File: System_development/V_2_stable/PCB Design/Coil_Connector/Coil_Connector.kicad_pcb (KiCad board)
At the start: 2 copper layers, 16.7 x 11.4 mm, 2 parts, among them J1 Conn_Coaxial

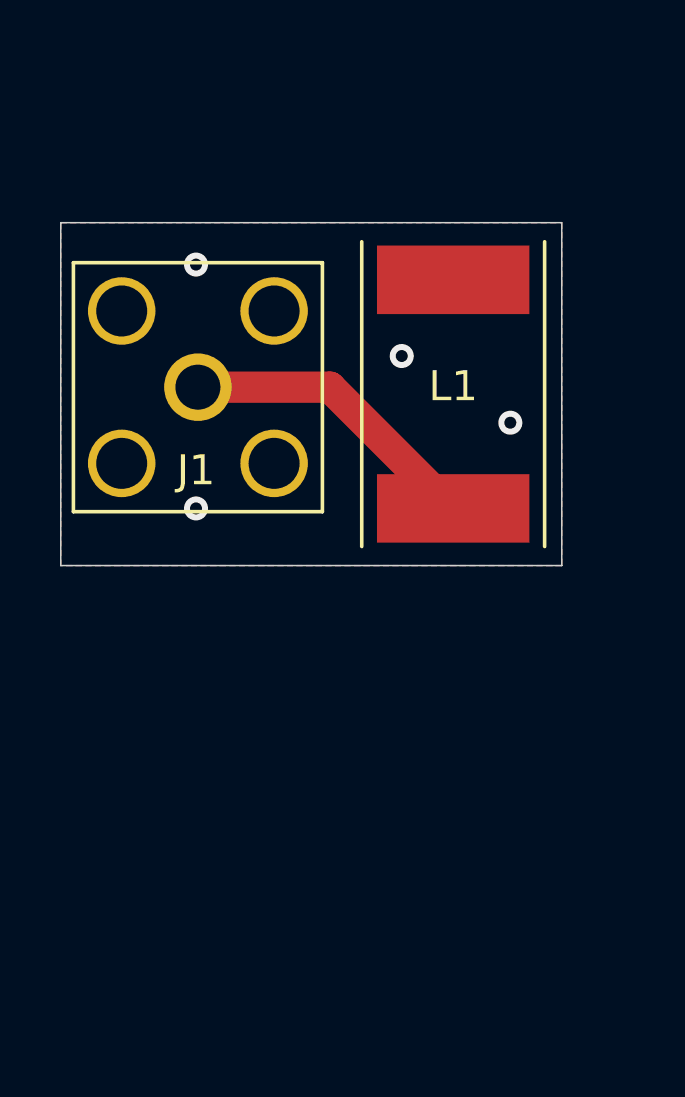
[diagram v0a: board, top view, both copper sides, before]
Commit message: Coil Connector PCB
Added screw holes
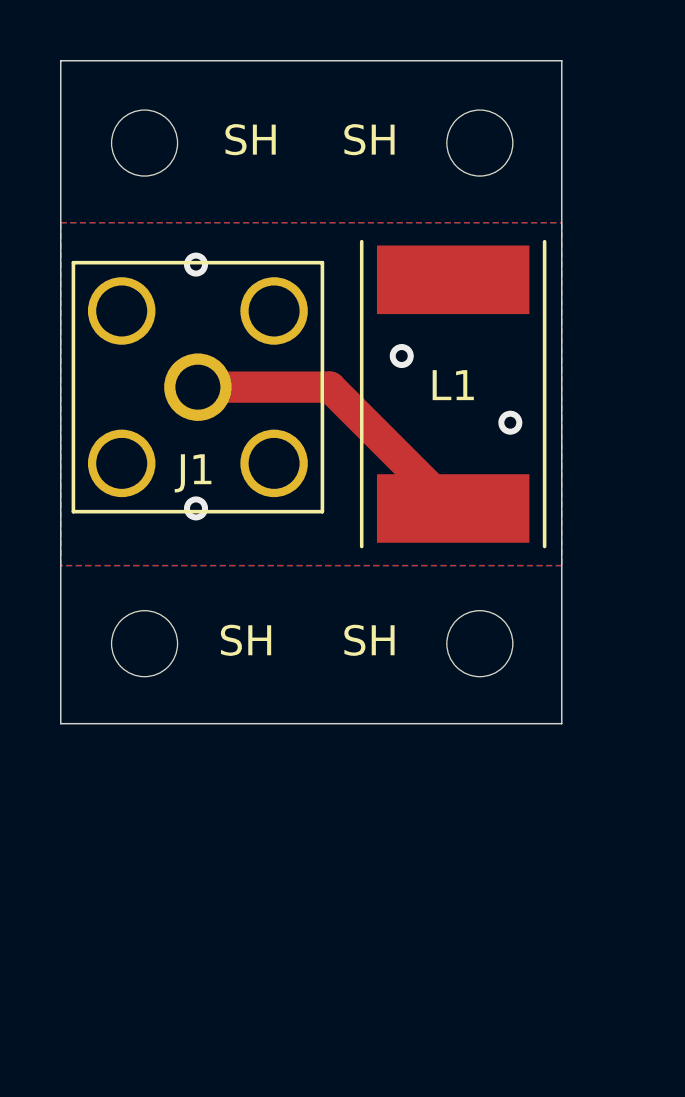
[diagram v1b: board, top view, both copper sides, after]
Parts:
- added SH: MountingHole_2.2mm_M2, MountingHole:MountingHole_2.2mm_M2, F.Cu at (144.8, 93.7)
- added SH: MountingHole_2.2mm_M2, MountingHole:MountingHole_2.2mm_M2, F.Cu at (133.6, 110.4)
- added SH: MountingHole_2.2mm_M2, MountingHole:MountingHole_2.2mm_M2, F.Cu at (133.6, 93.7)
- added SH: MountingHole_2.2mm_M2, MountingHole:MountingHole_2.2mm_M2, F.Cu at (144.8, 110.4)
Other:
- board size 16.7 x 11.4 mm -> 16.7 x 22.1 mm
- net class 50 Ohm removed
- net class Default removed

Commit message: Coil PCB & HP Amp PCB
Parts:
- removed the SH at (144.8, 93.7)
- removed the SH at (144.8, 110.4)
- moved SH 15.3 mm to (146.8, 101.3)
- moved SH 11.6 mm to (139.1, 120.7)
- moved L1 6.69 mm to (139.1, 109.5), turned to 180 degrees
- moved J1 3.70 mm to (139.1, 101.5)
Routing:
- net Net-(J1-Pad1): track 10.2 -> 6.98 mm
- net GND: vias 4 -> 3
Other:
- board size 16.7 x 22.1 mm -> 15.5 x 26.7 mm
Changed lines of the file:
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@@
   (net 2 "Net-(J1-Pad1)")
   (footprint "Connector_Coaxial:SMA_Amphenol_132203-12_Horizontal" (layer "F.Cu")
-    (at 135.382 101.813001)
+    (at 139.065 101.473)
     (descr "https://www.amphenolrf.com/media/downloads/1769/132203-12.pdf")
     (tags "SMA THT Female Jack Horizontal")
     (attr through_hole)
-    (fp_text reference "J1" (at -0.0635 2.771499 180) (layer "F.SilkS")
+    (fp_text reference "J1" (at -0.0635 -2.667 180) (layer "F.SilkS")
       (effects (font (size 1 1) (thickness 0.15)))
     )
@@
   )
   (footprint "L_Coil:L_Coil" (layer "F.Cu")
-    (at 143.891 104.8385)
+    (at 139.065 109.474 180)
     (attr through_hole)
     (fp_text reference "L1" (at 0 -3.056) (layer "F.SilkS")
@@
     (fp_line (start 3.302 2.54) (end -3.302 2.54) (layer "F.CrtYd") (width 0.12))
     (fp_line (start 3.302 -8.128) (end 3.302 2.54) (layer "F.CrtYd") (width 0.12))
-    (pad "1" smd rect locked (at 0 1.016) (size 5.08 2.286) (layers "F.Cu" "F.Paste" "F.Mask")
+    (pad "1" smd rect locked (at 0 1.016 180) (size 5.08 2.286) (layers "F.Cu" "F.Paste" "F.Mask")
       (net 2 "Net-(J1-Pad1)"))
-    (pad "2" smd rect locked (at 0 -6.604) (size 5.08 2.286) (layers "F.Cu" "F.Paste" "F.Mask")
+    (pad "2" smd rect locked (at 0 -6.604 180) (size 5.08 2.286) (layers "F.Cu" "F.Paste" "F.Mask")
       (net 1 "GND"))
   )
   (footprint "MountingHole:MountingHole_2.2mm_M2" (layer "F.Cu")
-    (at 144.78 93.6752)
-    (descr "Mounting Hole 2.2mm, no annular, M2")
-    (tags "mounting hole 2.2mm no annular m2")
-    (attr exclude_from_pos_files exclude_from_bom)
-    (fp_text reference "SH" (at -3.6576 -0.0762) (layer "F.SilkS")
-      (effects (font (size 1 1) (thickness 0.15)))
-    )
-    (fp_text value "MountingHole_2.2mm_M2" (at 0 3.2) (layer "F.Fab")
-      (effects (font (size 1 1) (thickness 0.15)))
-    )
-    (fp_text user "${REFERENCE}" (at 0.3 0) (layer "F.Fab")
-      (effects (font (size 1 1) (thickness 0.15)))
-    )
-    (fp_circle (center 0 0) (end 2.2 0) (layer "Cmts.User") (width 0.15) (fill none))
-    (fp_circle (center 0 0) (end 2.45 0) (layer "F.CrtYd") (width 0.05) (fill none))
-    (pad "" np_thru_hole circle (at 0 0) (size 2.2 2.2) (drill 2.2) (layers *.Cu *.Mask))
-  )
-  (footprint "MountingHole:MountingHole_2.2mm_M2" (layer "F.Cu")
-    (at 133.604 110.363)
+    (at 139.065 120.65)
     (descr "Mounting Hole 2.2mm, no annular, M2")
     (tags "mounting hole 2.2mm no annular m2")
@@
   )
   (footprint "MountingHole:MountingHole_2.2mm_M2" (layer "F.Cu")
-    (at 133.604 93.6752)
+    (at 146.812 101.346)
     (descr "Mounting Hole 2.2mm, no annular, M2")
     (tags "mounting hole 2.2mm no annular m2")
     (attr exclude_from_pos_files exclude_from_bom)
-    (fp_text reference "SH" (at 3.556 -0.0762) (layer "F.SilkS")
+    (fp_text reference "SH" (at 0 -3.302) (layer "F.SilkS")
       (effects (font (size 1 1) (thickness 0.15)))
     )
@@
     (pad "" np_thru_hole circle (at 0 0) (size 2.2 2.2) (drill 2.2) (layers *.Cu *.Mask))
   )
-  (footprint "MountingHole:MountingHole_2.2mm_M2" (layer "F.Cu")
-    (at 144.78 110.363)
-    (descr "Mounting Hole 2.2mm, no annular, M2")
-    (tags "mounting hole 2.2mm no annular m2")
-    (attr exclude_from_pos_files exclude_from_bom)
-    (fp_text reference "SH" (at -3.6576 -0.0762) (layer "F.SilkS")
-      (effects (font (size 1 1) (thickness 0.15)))
-    )
-    (fp_text value "MountingHole_2.2mm_M2" (at 0 3.2) (layer "F.Fab")
-      (effects (font (size 1 1) (thickness 0.15)))
-    )
-    (fp_text user "${REFERENCE}" (at 0.3 0) (layer "F.Fab")
-      (effects (font (size 1 1) (thickness 0.15)))
-    )
-    (fp_circle (center 0 0) (end 2.2 0) (layer "Cmts.User") (width 0.15) (fill none))
-    (fp_circle (center 0 0) (end 2.45 0) (layer "F.CrtYd") (width 0.05) (fill none))
-    (pad "" np_thru_hole circle (at 0 0) (size 2.2 2.2) (drill 2.2) (layers *.Cu *.Mask))
-  )
-  (gr_line (start 147.5105 113.03) (end 147.5105 90.932) (layer "Edge.Cuts") (width 0.05))
-  (gr_line (start 130.81 113.03) (end 147.5105 113.03) (layer "Edge.Cuts") (width 0.05))
-  (gr_line (start 130.81 90.932) (end 130.81 113.03) (layer "Edge.Cuts") (width 0.05))
-  (gr_line (start 147.5105 90.932) (end 130.81 90.932) (layer "Edge.Cuts") (width 0.05))
-  (via (at 145.796 102.997) (size 0.8) (drill 0.4) (layers "F.Cu" "B.Cu") (net 1))
-  (via (at 135.3185 97.7265) (size 0.8) (drill 0.4) (layers "F.Cu" "B.Cu") (net 1))
-  (via (at 135.3185 105.8545) (size 0.8) (drill 0.4) (layers "F.Cu" "B.Cu") (net 1))
-  (via (at 142.1765 100.7745) (size 0.8) (drill 0.4) (layers "F.Cu" "B.Cu") (net 1))
-  (segment (start 139.786001 101.813001) (end 143.891 105.918) (width 1.044) (layer "F.Cu") (net 2))
-  (segment (start 135.382 101.813001) (end 139.786001 101.813001) (width 1.044) (layer "F.Cu") (net 2))
+  (gr_line (start 149.606 96.774) (end 149.606 106.426) (layer "Edge.Cuts") (width 0.05))
+  (gr_line (start 149.606 106.426) (end 149.606 106.934) (layer "Edge.Cuts") (width 0.05))
+  (gr_line (start 144.018 106.934) (end 144.018 123.444) (layer "Edge.Cuts") (width 0.05))
+  (gr_line (start 134.112 96.774) (end 149.606 96.774) (layer "Edge.Cuts") (width 0.05))
+  (gr_line (start 144.018 123.444) (end 134.112 123.444) (layer "Edge.Cuts") (width 0.05))
+  (gr_line (start 149.606 106.934) (end 144.018 106.934) (layer "Edge.Cuts") (width 0.05))
+  (gr_line (start 134.112 123.444) (end 134.112 96.774) (layer "Edge.Cuts") (width 0.05))
+  (via (at 141.732 101.346) (size 0.8) (drill 0.4) (layers "F.Cu" "B.Cu") (free) (net 1))
+  (via (at 136.398 101.346) (size 0.8) (drill 0.4) (layers "F.Cu" "B.Cu") (free) (net 1))
+  (via (at 138.938 111.252) (size 0.8) (drill 0.4) (layers "F.Cu" "B.Cu") (free) (net 1))
+  (segment (start 139.065 101.473) (end 139.065 108.458) (width 1.044) (layer "F.Cu") (net 2))
   (zone (net 1) (net_name "GND") (layer "F.Cu") (hatch edge 0.508)
     (connect_pads (clearance 0.508))
@@
     (polygon
       (pts
-        (xy 147.5105 107.7595)
-        (xy 130.81 107.7595)
-        (xy 130.81 96.3295)
-        (xy 147.5105 96.3295)
+        (xy 143.764 117.856)
+        (xy 134.366 117.856)
+        (xy 134.366 97.028)
+        (xy 143.764 97.028)
       )
     )
@@
     (polygon
       (pts
-        (xy 147.5105 107.7595)
-        (xy 130.81 107.7595)
-        (xy 130.81 96.3295)
-        (xy 147.5105 96.3295)
+        (xy 143.764 117.856)
+        (xy 134.366 117.856)
+        (xy 134.366 97.028)
+        (xy 143.764 97.028)
       )
     )
